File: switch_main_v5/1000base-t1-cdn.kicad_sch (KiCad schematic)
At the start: 9 parts, among them T1801 74930100

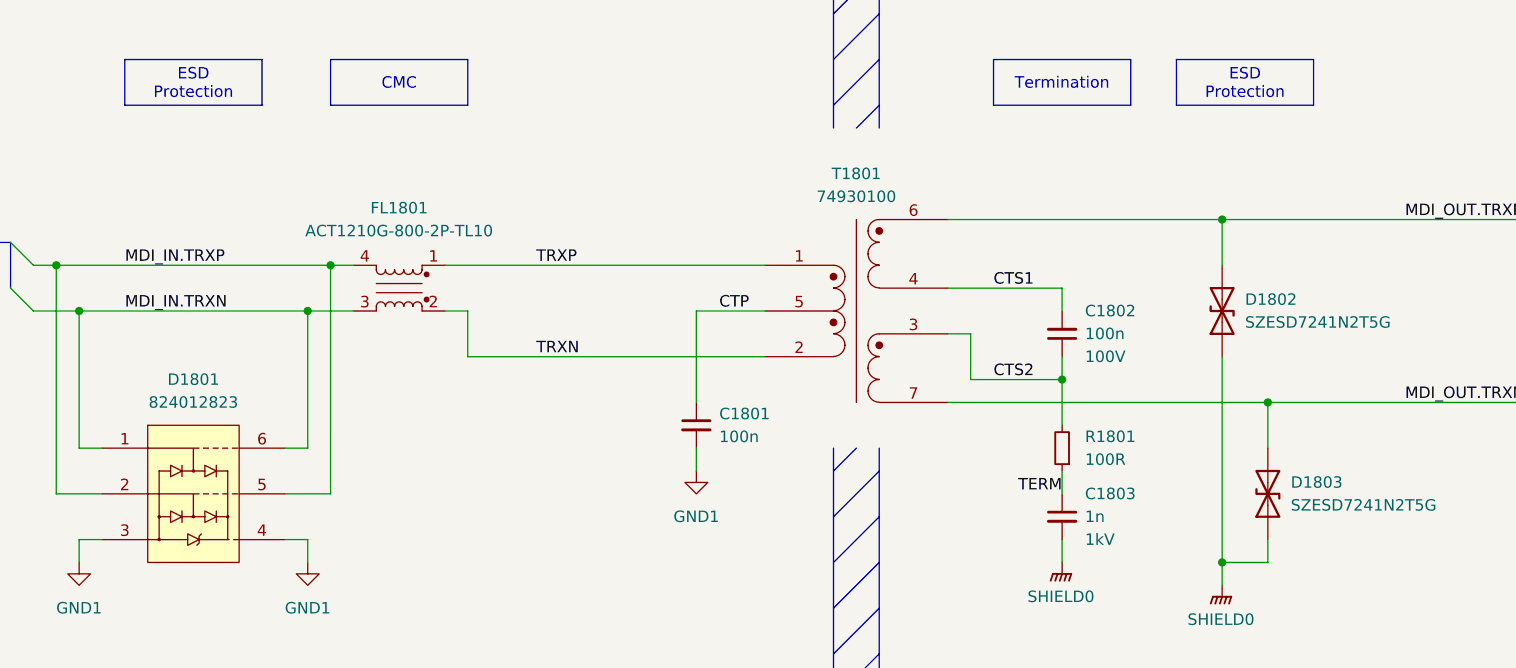
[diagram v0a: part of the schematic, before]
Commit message: MDIO multiplexing
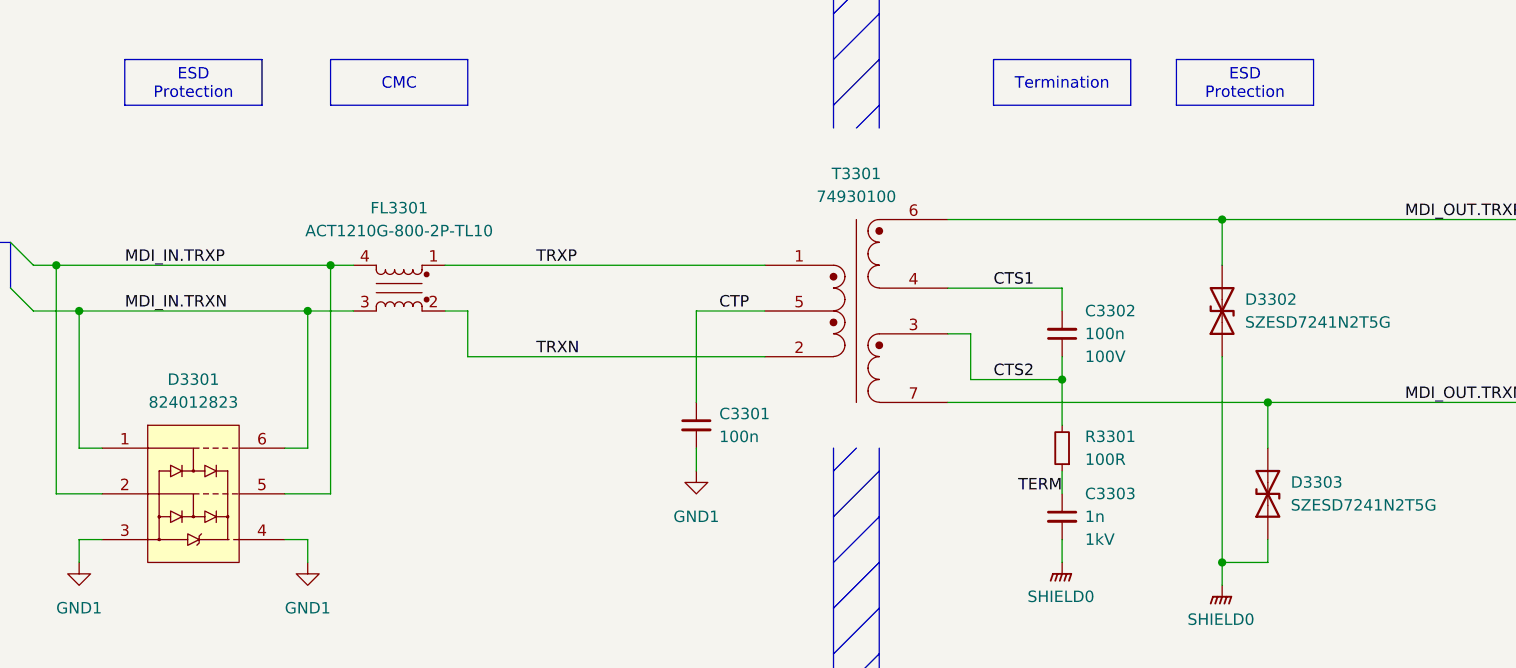
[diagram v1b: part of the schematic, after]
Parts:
- renumbered C1801 to C3301, C1802 to C3302, C1803 to C3303, D1801 to D3301, D1802 to D3302, D1803 to D3303, FL1801 to FL3301, R1801 to R3301, T1801 to T3301

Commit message: Updated 1v0_buck_converter feedback resistors
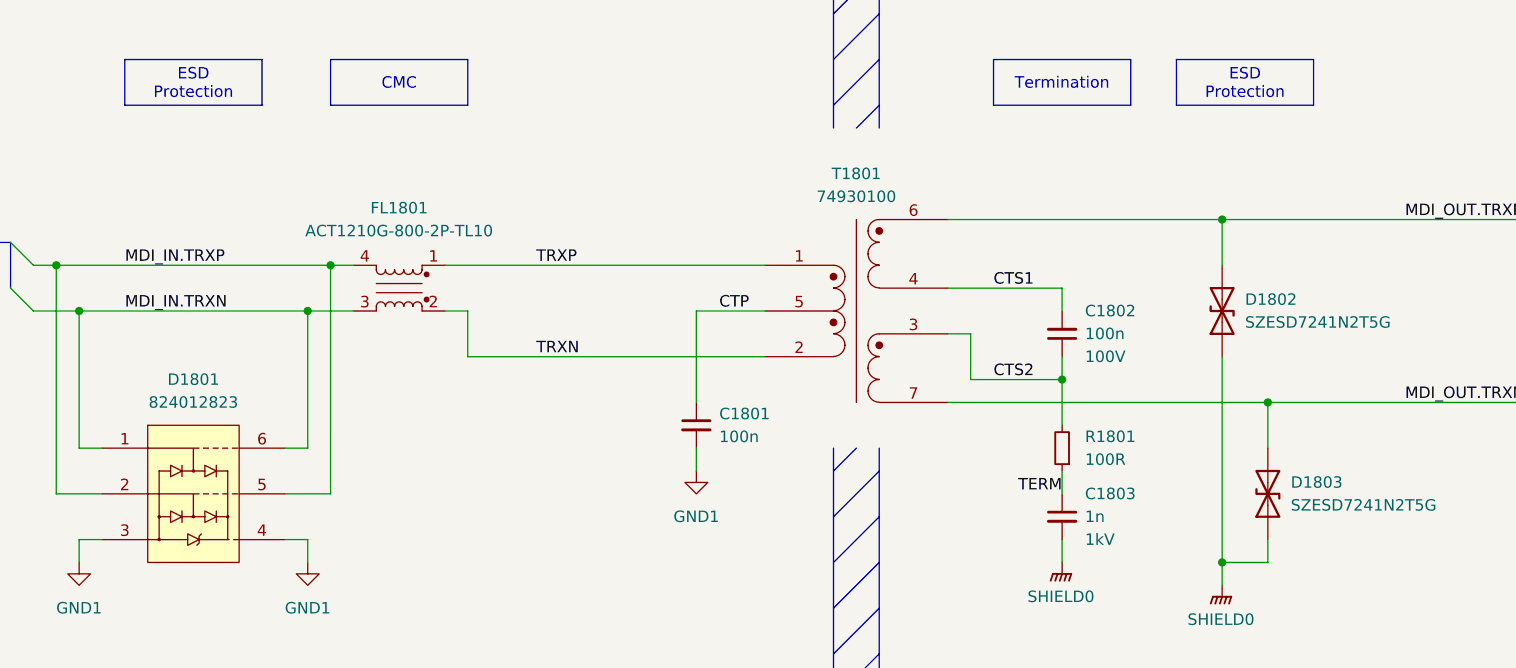
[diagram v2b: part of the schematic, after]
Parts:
- renumbered C3301 to C1801, C3302 to C1802, C3303 to C1803, D3301 to D1801, D3302 to D1802, D3303 to D1803, FL3301 to FL1801, R3301 to R1801, T3301 to T1801
